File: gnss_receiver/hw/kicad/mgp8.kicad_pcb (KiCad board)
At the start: 8 copper layers, 100 x 75 mm, 429 parts, among them X1 FTSH-105-01-L-DV-K, X2 FTSH-105-01-L-DV-K, X3 FTSH-105-01-L-DV-K, X4 M22-2510205, X5 SM06B-GHS-TB, X6 SM04B-GHS-TB, X7 SM04B-GHS-TB, X8 SM04B-SRSS-TB

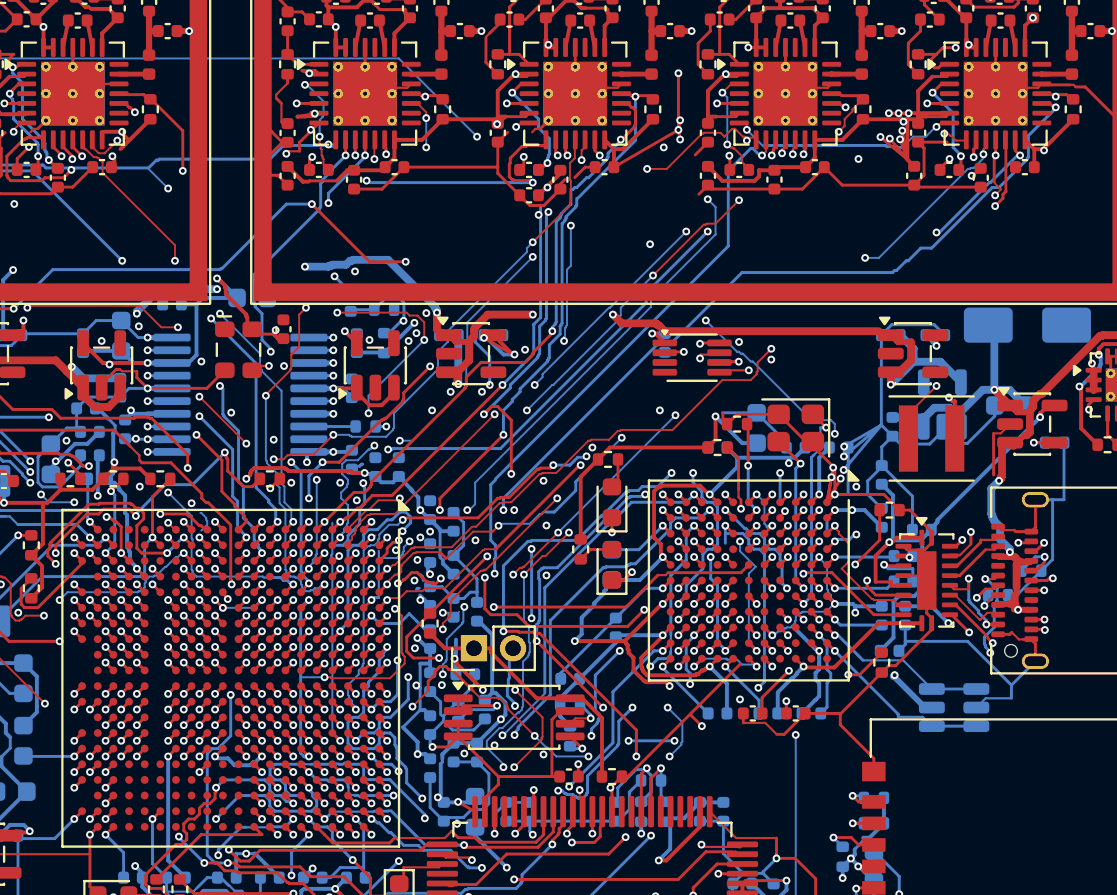
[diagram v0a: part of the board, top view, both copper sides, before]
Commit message: МГП-8: сняты висящие отрезки и переходы платы — DRC без ошибок и без висящих
9 одиночных переходов, соединявших два проводника одного слоя, заменены
отрезками; 14 отводов обрезаны по точке примыкания. Связность в KiCad
проверялась после каждой правки: неразведённых 0, расхождений со схемой 0.
DRC: ошибок нет, из предупреждений — 3 наложения шелкографии.
Проводников 9312, переходов 1311, 10,64 м; масса и тепловой расчёт те же.
ПЗ 4.7.4, CLAUDE.md, КД ПЗ.

Co-Authored-By: Claude Opus 5.5 <noreply@anthropic.com>
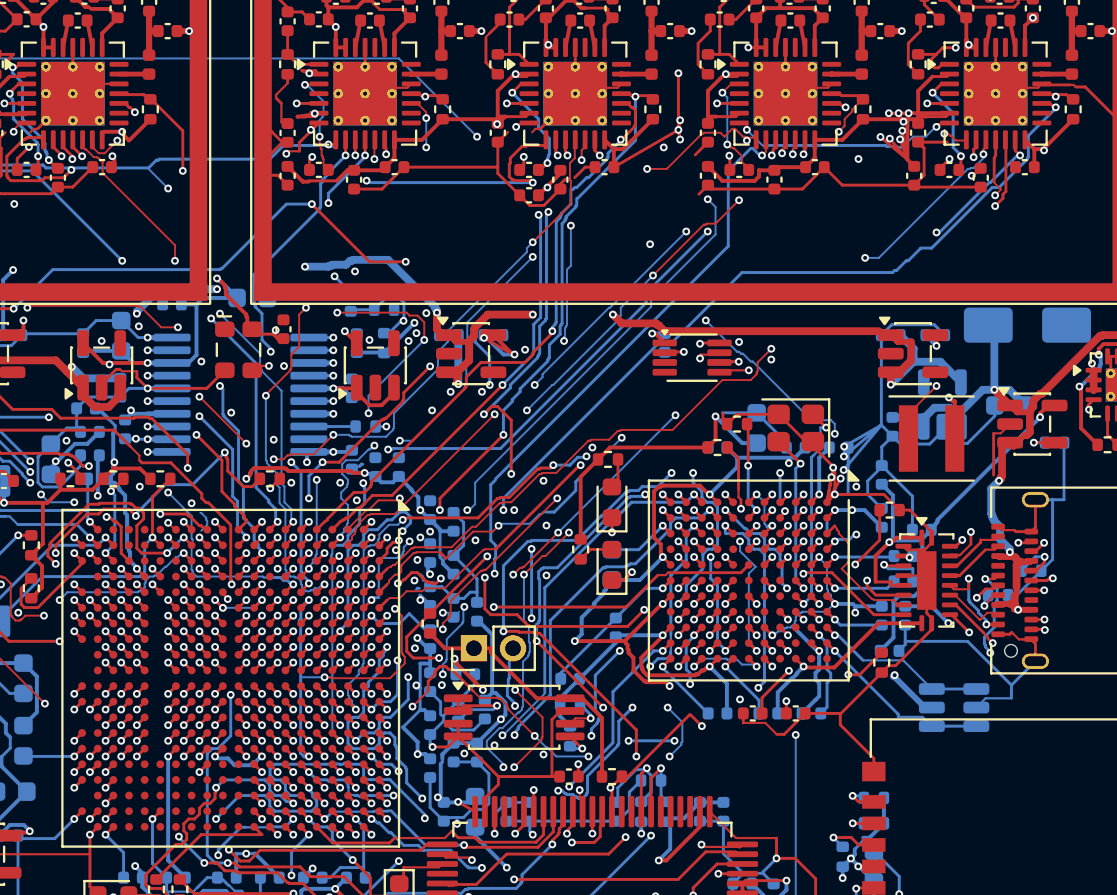
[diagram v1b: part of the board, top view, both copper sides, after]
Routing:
- net FX3_RESETN: track 26.1 -> 22.5 mm
- net FX3_G13: track 23.6 -> 21.8 mm
- net FX3_G35: track 23.6 -> 22.4 mm
- net FX3_LOCK_E: track 39.3 -> 38.1 mm
- net MAX_LD_H: track 49.7 -> 48.7 mm
- net +3V3D: track 234.0 -> 233.1 mm
- net FX3_G14: track 25.3 -> 24.6 mm
- net +3V3_RF2: track 56.7 -> 56.1 mm
- net MAX_LD_G: track 44.1 -> 43.5 mm
- net MAX_I1_F: track 26.8 -> 26.5 mm, vias 4 -> 3
- net MAX_Q0_H: track 43.5 -> 43.8 mm, vias 5 -> 3
- net SSRX_N: track 6.53 -> 6.71 mm, vias 1 -> 0
- net MAX_Q1_H: track 40.4 -> 40.6 mm, vias 4 -> 3
- net MAX_LD_F: track 30.0 -> 30.2 mm, vias 3 -> 2
- net MAX_CSN_H: track 42.5 -> 42.7 mm, vias 3 -> 2
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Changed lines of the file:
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@@
 	)
 	(segment
-		(start 105.9 94.15)
+		(start 106.175 93.875)
 		(end 106.55 93.5)
 		(width 0.15)
@@
 	)
 	(segment
-		(start 94.3625 73.9375)
+		(start 94.8 73.5)
 		(end 95.89 72.41)
 		(width 0.2)
@@
 	)
 	(segment
+		(start 108 95.4)
+		(end 108.15 95.3)
+		(width 0.1)
+		(locked yes)
+		(layer "F.Cu")
+		(net "MAX_Q1_H")
+	)
+	(segment
 		(start 118.45 88.8)
 		(end 119.35 88.8)
@@
 	)
 	(via
-		(at 108 95.4)
-		(size 0.4)
-		(drill 0.2)
-		(layers "F.Cu" "B.Cu")
-		(locked yes)
-		(net "MAX_Q1_H")
-	)
-	(via
 		(at 138.5 74.2)
 		(size 0.4)
@@
 	)
 	(segment
+		(start 108 96.199999)
+		(end 108.1 96.1)
+		(width 0.1)
+		(locked yes)
+		(layer "F.Cu")
+		(net "MAX_Q0_H")
+	)
+	(segment
 		(start 108.1 96)
 		(end 108.4 95.7)
@@
 	)
 	(segment
+		(start 139.125 74.26)
+		(end 139.05 74.4)
+		(width 0.15)
+		(locked yes)
+		(layer "F.Cu")
+		(net "MAX_Q0_H")
+	)
+	(segment
 		(start 139.125 73.4625)
 		(end 139.125 74.26)
@@
 	)
 	(via
-		(at 139.125 74.26)
-		(size 0.4)
-		(drill 0.2)
-		(layers "F.Cu" "B.Cu")
-		(locked yes)
-		(net "MAX_Q0_H")
-	)
-	(via
-		(at 108 96.199999)
-		(size 0.4)
-		(drill 0.2)
-		(layers "F.Cu" "B.Cu")
-		(locked yes)
-		(net "MAX_Q0_H")
-	)
-	(via
 		(at 139.1 76.3)
 		(size 0.4)
@@
 	)
 	(segment
+		(start 108 97)
+		(end 108.15 96.9)
+		(width 0.1)
+		(locked yes)
+		(layer "F.Cu")
+		(net "FX3_G0")
+	)
+	(segment
 		(start 108.65 96.9)
 		(end 109 96.55)
@@
 		(net "FX3_G0")
 	)
-	(via
-		(at 108 97)
-		(size 0.4)
-		(drill 0.2)
-		(layers "F.Cu" "B.Cu")
-		(locked yes)
-		(net "FX3_G0")
-	)
 	(segment
 		(start 126.05 94.5)
@@
 	)
 	(segment
-		(start 118.051 99.2058)
+		(start 119.9 99.2058)
 		(end 122.494 99.2058)
 		(width 0.15)
@@
 	(segment
 		(start 110.35 93.1)
-		(end 109.85 93.1)
+		(end 110.2 93.1)
 		(width 0.15)
 		(locked yes)
@@
 	)
 	(segment
-		(start 109.55 93.4)
+		(start 110.2 93.4)
 		(end 112.95 93.4)
 		(width 0.15)
@@
 		(net "MAX_CSN_H")
 	)
-	(via
-		(at 121.95 87.3)
-		(size 0.4)
-		(drill 0.2)
-		(layers "F.Cu" "B.Cu")
-		(locked yes)
-		(net "MAX_CSN_H")
-	)
 	(segment
 		(start 129.35 79.9)
@@
 	)
 	(segment
+		(start 121.95 87.3)
+		(end 121.8 87.2)
+		(width 0.15)
+		(locked yes)
+		(layer "In5.Cu")
+		(net "MAX_CSN_H")
+	)
+	(segment
 		(start 133.35 79.05)
 		(end 138 74.4)
@@
 	(segment
 		(start 107.5752 96.8748)
-		(end 107.5752 94.4942)
+		(end 107.5752 94.85)
 		(width 0.1124)
 		(layer "B.Cu")
@@
 	(segment
 		(start 112.8144 94.3922)
-		(end 108.9205 94.3922)
+		(end 109.25 94.3922)
 		(width 0.15)
 		(layer "In5.Cu")
@@
 	)
 	(segment
-		(start 110.7 97.25)
+		(start 111.95 97.25)
 		(end 113 97.25)
 		(width 0.15)
@@
 	)
 	(segment
-		(start 125.3 94.0922)
+		(start 125.3 93.6)
 		(end 125.3 93.2)
 		(width 0.15)
@@
 	(segment
 		(start 123.2 78.8)
-		(end 124.25 77.75)
+		(end 123.85 78.15)
 		(width 0.15)
 		(locked yes)
@@
 		(net "MAX_I1_F")
 	)
-	(via
-		(at 105.6 93)
-		(size 0.4)
-		(drill 0.2)
-		(layers "F.Cu" "B.Cu")
+	(segment
+		(start 105.6 93)
+		(end 105.75 92.9)
+		(width 0.15)
 		(locked yes)
+		(layer "F.Cu")
 		(net "MAX_I1_F")
 	)
@@
 	(segment
 		(start 115.85 82.55)
-		(end 115.85 76.8)
+		(end 115.85 77.3)
 		(width 0.15)
 		(locked yes)
@@
 	(segment
 		(start 105.2 94.65)
-		(end 105.2 93.05)
+		(end 105.2 94.2)
 		(width 0.1)
 		(locked yes)
@@
 	)
 	(segment
+		(start 104.8 93)
+		(end 104.95 92.9)
+		(width 0.15)
+		(locked yes)
+		(layer "F.Cu")
+		(net "MAX_LD_F")
+	)
+	(segment
 		(start 120.5 71.8)
 		(end 120.4 71.7)
@@
 	)
 	(via
-		(at 104.8 93)
-		(size 0.4)
-		(drill 0.2)
-		(layers "F.Cu" "B.Cu")
-		(locked yes)
-		(net "MAX_LD_F")
-	)
-	(via
 		(at 116.45 83.25)
 		(size 0.4)
@@
 	(segment
 		(start 111.52 100.8)
-		(end 111.52 99.0243)
+		(end 111.52 100)
 		(width 0.2)
 		(layer "B.Cu")
@@
 	)
 	(segment
+		(start 94.4 94.6)
+		(end 94.4 94.45)
+		(width 0.15)
+		(locked yes)
+		(layer "F.Cu")
+		(net "FLASH_CLK")
+	)
+	(segment
 		(start 93.8 92.75)
 		(end 93.65 92.75)
@@
 		(net "FLASH_CLK")
 	)
-	(via
-		(at 94.4 94.6)
-		(size 0.4)
-		(drill 0.2)
-		(layers "F.Cu" "B.Cu")
-		(locked yes)
-		(net "FLASH_CLK")
-	)
 	(segment
 		(start 86.25 91.9)
@@
 	)
 	(segment
-		(start 126.073 100.267)
+		(start 123.494999 102.845)
 		(end 120.31 106.03)
 		(width 0.15)
@@
 	)
 	(segment
+		(start 130.9 93.199999)
+		(end 131 93.35)
+		(width 0.1)
+		(locked yes)
+		(layer "F.Cu")
+		(net "SSRX_N")
+	)
+	(segment
 		(start 132.9 97)
 		(end 133.9 97)
@@
 		(net "SSRX_N")
 	)
-	(via
-		(at 130.9 93.199999)
-		(size 0.4)
-		(drill 0.2)
-		(layers "F.Cu" "B.Cu")
-		(locked yes)
-		(net "SSRX_N")
-	)
